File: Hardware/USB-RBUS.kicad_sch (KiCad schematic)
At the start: 8 parts, among them J4 USB_C_Receptacle_USB2.0

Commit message: PCB mid design
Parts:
- removed D6: SP0503BAHT, Package_TO_SOT_SMD:SOT-143, symbol Power_Protection:SP0503BAHT
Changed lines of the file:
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@@
-	(wire
-		(pts
-			(xy 124.46 91.44) (xy 124.46 97.79)
-		)
-		(stroke
-			(width 0)
-			(type default)
-		)
-	)
 	(wire
 		(pts
@@
 			)
 			(justify left bottom)
-		)
-	)
-	(label "CAN+"
-		(at 129.54 97.79 90)
-		(fields_autoplaced yes)
-		(effects
-			(font
-				(size 1.27 1.27)
-			)
-			(justify left bottom)
-		)
-	)
-	(label "CAN-"
-		(at 127 97.79 90)
-		(fields_autoplaced yes)
-		(effects
-			(font
-				(size 1.27 1.27)
-			)
-			(justify left bottom)
-		)
-	)
-	(global_label "RBUS_uC_V"
-		(shape input)
-		(at 124.46 91.44 90)
-		(fields_autoplaced yes)
-		(effects
-			(font
-				(size 1.27 1.27)
-			)
-			(justify left)
-		)
-		(property "Intersheetrefs" "${INTERSHEET_REFS}"
-			(at 124.46 78.5862 90)
-			(effects
-				(font
-					(size 1.27 1.27)
-				)
-				(justify left)
-				(hide yes)
-			)
 		)
 	)
@@
 					(unit 1)
 				)
-			)
-		)
-	)
-	(symbol
-		(lib_id "power:GND")
-		(at 127 107.95 0)
-		(unit 1)
-		(exclude_from_sim no)
-		(in_bom yes)
-		(on_board yes)
-		(dnp no)
-		(property "Reference" "#PWR062"
-			(at 127 114.3 0)
-			(effects
-				(font
-					(size 1.27 1.27)
-				)
-				(hide yes)
-			)
-		)
-		(property "Value" "GND"
-			(at 127.127 112.3442 0)
-			(effects
-				(font
-					(size 1.27 1.27)
-				)
-			)
-		)
-		(property "Footprint" ""
-			(at 127 107.95 0)
-			(effects
-				(font
-					(size 1.27 1.27)
-				)
-				(hide yes)
-			)
-		)
-		(property "Datasheet" ""
-			(at 127 107.95 0)
-			(effects
-				(font
-					(size 1.27 1.27)
-				)
-				(hide yes)
-			)
-		)
-		(property "Description" ""
-			(at 127 107.95 0)
-			(effects
-				(font
-					(size 1.27 1.27)
-				)
-				(hide yes)
-			)
-		)
-		(pin "1"
-		)
-		(instances
-			(project "Main board"
-				(path "/7db990e4-92e1-4f99-b4d2-435bbec1ba83/3151accb-1938-449b-8397-baa4e59e1635"
-					(reference "#PWR062")
-					(unit 1)
-				)
-			)
-		)
-	)
-	(symbol
-		(lib_id "Power_Protection:SP0503BAHT")
-		(at 127 102.87 0)
-		(unit 1)
-		(exclude_from_sim no)
-		(in_bom yes)
-		(on_board yes)
-		(dnp no)
-		(property "Reference" "D6"
-			(at 132.207 101.7016 0)
-			(effects
-				(font
-					(size 1.27 1.27)
-				)
-				(justify left)
-			)
-		)
-		(property "Value" "SP0503BAHT"
-			(at 132.207 104.013 0)
-			(effects
-				(font
-					(size 1.27 1.27)
-				)
-				(justify left)
-			)
-		)
-		(property "Footprint" "Package_TO_SOT_SMD:SOT-143"
-			(at 132.715 104.14 0)
-			(effects
-				(font
-					(size 1.27 1.27)
-				)
-				(justify left)
-				(hide yes)
-			)
-		)
-		(property "Datasheet" "http://www.littelfuse.com/~/media/files/littelfuse/technical%20resources/documents/data%20sheets/sp05xxba.pdf"
-			(at 130.175 99.695 0)
-			(effects
-				(font
-					(size 1.27 1.27)
-				)
-				(hide yes)
-			)
-		)
-		(property "Description" ""
-			(at 127 102.87 0)
-			(effects
-				(font
-					(size 1.27 1.27)
-				)
-				(hide yes)
-			)
-		)
-		(pin "1"
-		)
-		(pin "2"
-		)
-		(pin "3"
-		)
-		(pin "4"
-		)
-		(instances
-			(project "Main board"
-				(path "/7db990e4-92e1-4f99-b4d2-435bbec1ba83/3151accb-1938-449b-8397-baa4e59e1635"
-					(reference "D6")
-					(unit 1)
-				)

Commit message: Crosshair V1.0
New pyro connectors, silkscreen sorted, mostly connected properly + cool new name and image
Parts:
- J4: footprint Connector_USB:USB_C_Receptacle_Palconn_UTC16-G -> iclr:USB_C_Receptacle_Palconn_UTC16-G
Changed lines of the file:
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@@
 (kicad_sch
-	(version 20231120)
+	(version 20250114)
 	(generator "eeschema")
-	(generator_version "8.0")
+	(generator_version "9.0")
 	(paper "A4")
 	(junction
@@
 	(label "CAN+"
 		(at 39.37 67.31 0)
-		(fields_autoplaced yes)
 		(effects
 			(font
@@
 	(label "CAN-"
 		(at 111.76 66.04 0)
-		(fields_autoplaced yes)
 		(effects
 			(font
@@
 	(label "CAN-"
 		(at 39.37 62.23 0)
-		(fields_autoplaced yes)
 		(effects
 			(font
@@
 	(label "CAN+"
 		(at 111.76 71.12 0)
-		(fields_autoplaced yes)
 		(effects
 			(font
@@
 		(shape bidirectional)
 		(at 39.37 67.31 180)
-		(fields_autoplaced yes)
 		(effects
 			(font
@@
 		(shape bidirectional)
 		(at 39.37 62.23 180)
-		(fields_autoplaced yes)
 		(effects
 			(font
@@
 			)
 		)
-		(property "Footprint" "Connector_USB:USB_C_Receptacle_Palconn_UTC16-G"
+		(property "Footprint" "iclr:USB_C_Receptacle_Palconn_UTC16-G"
 			(at 99.06 67.31 0)
 			(effects

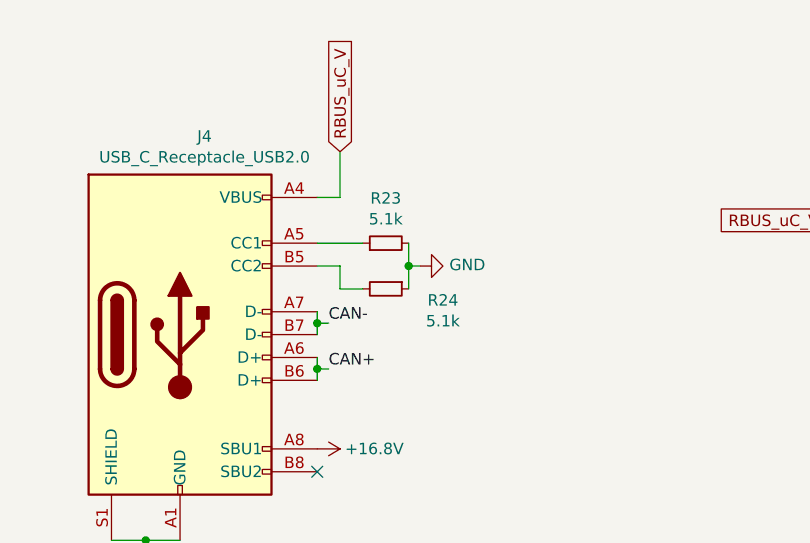
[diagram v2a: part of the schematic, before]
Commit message: Crosshair post review 2
Layout redesign + changes implemented. Traces not yet complete
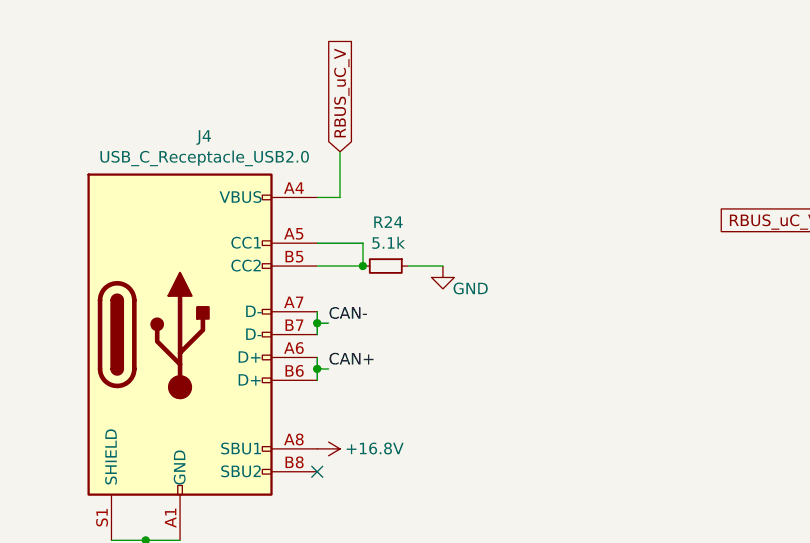
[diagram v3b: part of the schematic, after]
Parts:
- removed R23: 5.1k, Resistor_SMD:R_0402_1005Metric, symbol Device:R_Small
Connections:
- net at J4.A5 (CC1): now also J4.B5 (CC2), R24.2
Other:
- moved on the sheet: R24
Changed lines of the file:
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@@
 	)
 	(junction
-		(at 120.65 59.69)
+		(at 115.57 59.69)
 		(diameter 0)
 		(color 0 0 0 0)
@@
 	(wire
 		(pts
-			(xy 110.49 59.69) (xy 113.03 59.69)
+			(xy 110.49 59.69) (xy 115.57 59.69)
 		)
 		(stroke
@@
 	(wire
 		(pts
-			(xy 120.65 59.69) (xy 121.92 59.69)
+			(xy 120.65 59.69) (xy 124.46 59.69)
+		)
+		(stroke
+			(width 0)
+			(type default)
+		)
+	)
+	(wire
+		(pts
+			(xy 115.57 57.15) (xy 115.57 59.69)
 		)
 		(stroke
@@
 	(wire
 		(pts
-			(xy 113.03 62.23) (xy 115.57 62.23)
-		)
-		(stroke
-			(width 0)
-			(type default)
-		)
-	)
-	(wire
-		(pts
-			(xy 120.65 57.15) (xy 120.65 59.69)
-		)
-		(stroke
-			(width 0)
-			(type default)
-		)
-	)
-	(wire
-		(pts
 			(xy 110.49 71.12) (xy 110.49 72.39)
 		)
@@
 	(wire
 		(pts
-			(xy 113.03 59.69) (xy 113.03 62.23)
-		)
-		(stroke
-			(width 0)
-			(type default)
-		)
-	)
-	(wire
-		(pts
 			(xy 87.63 90.17) (xy 91.44 90.17)
 		)
@@
 		(pts
 			(xy 110.49 69.85) (xy 110.49 71.12)
-		)
-		(stroke
-			(width 0)
-			(type default)
-		)
-	)
-	(wire
-		(pts
-			(xy 120.65 62.23) (xy 120.65 59.69)
 		)
 		(stroke
@@
 			)
 			(justify right)
-		)
-	)
-	(symbol
-		(lib_id "Device:R_Small")
-		(at 118.11 57.15 90)
-		(unit 1)
-		(exclude_from_sim no)
-		(in_bom yes)
-		(on_board yes)
-		(dnp no)
-		(property "Reference" "R23"
-			(at 118.11 52.1716 90)
-			(effects
-				(font
-					(size 1.27 1.27)
-				)
-			)
-		)
-		(property "Value" "5.1k"
-			(at 118.11 54.483 90)
-			(effects
-				(font
-					(size 1.27 1.27)
-				)
-			)
-		)
-		(property "Footprint" "Resistor_SMD:R_0402_1005Metric"
-			(at 118.11 57.15 0)
-			(effects
-				(font
-					(size 1.27 1.27)
-				)
-				(hide yes)
-			)
-		)
-		(property "Datasheet" "~"
-			(at 118.11 57.15 0)
-			(effects
-				(font
-					(size 1.27 1.27)
-				)
-				(hide yes)
-			)
-		)
-		(property "Description" ""
-			(at 118.11 57.15 0)
-			(effects
-				(font
-					(size 1.27 1.27)
-				)
-				(hide yes)
-			)
-		)
-		(pin "1"
-		)
-		(pin "2"
-		)
-		(instances
-			(project "Main board"
-				(path "/7db990e4-92e1-4f99-b4d2-435bbec1ba83/3151accb-1938-449b-8397-baa4e59e1635"
-					(reference "R23")
-					(unit 1)
-				)
-			)
 		)
 	)
@@
 	(symbol
 		(lib_id "power:GND")
-		(at 121.92 59.69 90)
+		(at 124.46 59.69 0)
 		(unit 1)
 		(exclude_from_sim no)
@@
 		(dnp no)
 		(property "Reference" "#PWR060"
-			(at 128.27 59.69 0)
+			(at 124.46 66.04 0)
 			(effects
 				(font
@@
 		)
 		(property "Value" "GND"
-			(at 125.1712 59.563 90)
+			(at 129.54 62.23 0)
 			(effects
 				(font
@@
 		)
 		(property "Footprint" ""
-			(at 121.92 59.69 0)
+			(at 124.46 59.69 0)
 			(effects
 				(font
@@
 		)
 		(property "Datasheet" ""
-			(at 121.92 59.69 0)
+			(at 124.46 59.69 0)
 			(effects
 				(font
@@
 		)
 		(property "Description" ""
-			(at 121.92 59.69 0)
+			(at 124.46 59.69 0)
 			(effects
 				(font
@@
 	(symbol
 		(lib_id "Device:R_Small")
-		(at 118.11 62.23 270)
+		(at 118.11 59.69 270)
 		(unit 1)
 		(exclude_from_sim no)
@@
 		(dnp no)
 		(property "Reference" "R24"
-			(at 124.46 63.5 90)
+			(at 118.364 54.864 90)
 			(effects
 				(font
@@
 		)
 		(property "Value" "5.1k"
-			(at 124.46 65.8114 90)
+			(at 118.364 57.1754 90)
 			(effects
 				(font
@@
 		)
 		(property "Footprint" "Resistor_SMD:R_0402_1005Metric"
-			(at 118.11 62.23 0)
+			(at 118.11 59.69 0)
 			(effects
 				(font
@@
 		)
 		(property "Datasheet" "~"
-			(at 118.11 62.23 0)
+			(at 118.11 59.69 0)
 			(effects
 				(font
@@
 		)
 		(property "Description" ""
-			(at 118.11 62.23 0)
-			(effects
-				(font
+			(at 118.11 59.69 0)
+			(effects
+				(font

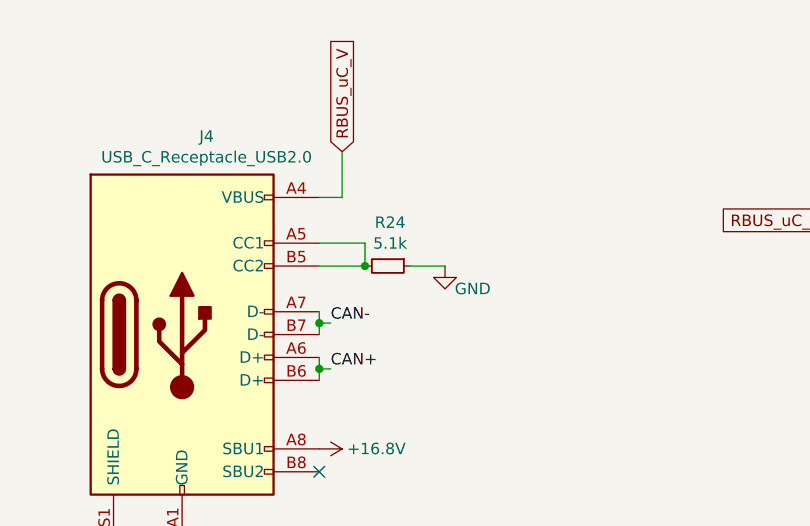
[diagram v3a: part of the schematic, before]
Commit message: I2C 'bus' sorted
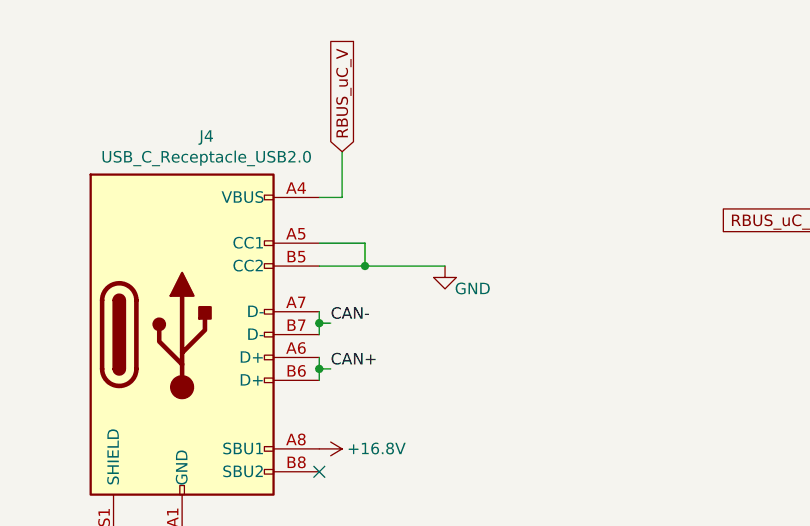
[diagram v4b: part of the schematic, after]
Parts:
- removed R24: 5.1k, Resistor_SMD:R_0402_1005Metric, symbol Device:R_Small
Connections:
- net GND: now also J4.A5 (CC1), J4.B5 (CC2)
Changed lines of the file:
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@@
+	)
+	(junction
+		(at 110.49 71.12)
+		(diameter 0)
+		(color 0 0 0 0)
 	)
 	(junction
@@
 	)
 	(junction
-		(at 110.49 71.12)
-		(diameter 0)
-		(color 0 0 0 0)
-	)
-	(junction
 		(at 91.44 90.17)
 		(diameter 0)
@@
 	(wire
 		(pts
-			(xy 120.65 59.69) (xy 124.46 59.69)
-		)
-		(stroke
-			(width 0)
-			(type default)
-		)
-	)
-	(wire
-		(pts
 			(xy 115.57 57.15) (xy 115.57 59.69)
 		)
@@
 		(pts
 			(xy 110.49 67.31) (xy 110.49 66.04)
+		)
+		(stroke
+			(width 0)
+			(type default)
+		)
+	)
+	(wire
+		(pts
+			(xy 115.57 59.69) (xy 124.46 59.69)
 		)
 		(stroke
@@
 					(unit 1)
 				)
-			)
-		)
-	)
-	(symbol
-		(lib_id "Device:R_Small")
-		(at 118.11 59.69 270)
-		(unit 1)
-		(exclude_from_sim no)
-		(in_bom yes)
-		(on_board yes)
-		(dnp no)
-		(property "Reference" "R24"
-			(at 118.364 54.864 90)
-			(effects
-				(font
-					(size 1.27 1.27)
-				)
-			)
-		)
-		(property "Value" "5.1k"
-			(at 118.364 57.1754 90)
-			(effects
-				(font
-					(size 1.27 1.27)
-				)
-			)
-		)
-		(property "Footprint" "Resistor_SMD:R_0402_1005Metric"
-			(at 118.11 59.69 0)
-			(effects
-				(font
-					(size 1.27 1.27)
-				)
-				(hide yes)
-			)
-		)
-		(property "Datasheet" "~"
-			(at 118.11 59.69 0)
-			(effects
-				(font
-					(size 1.27 1.27)
-				)
-				(hide yes)
-			)
-		)
-		(property "Description" ""
-			(at 118.11 59.69 0)
-			(effects
-				(font
-					(size 1.27 1.27)
-				)
-				(hide yes)
-			)
-		)
-		(pin "1"
-		)
-		(pin "2"
-		)
-		(instances
-			(project "Main board"
-				(path "/7db990e4-92e1-4f99-b4d2-435bbec1ba83/3151accb-1938-449b-8397-baa4e59e1635"
-					(reference "R24")
-					(unit 1)
-				)

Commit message: Mega commit
Post review changes
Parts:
- RBUSLED: renamed from USBLED2; footprint Resistor_SMD:R_0402_1005Metric -> LED_SMD:LED_0402_1005Metric
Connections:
- net +16.8V: now also J4.A4 (VBUS), J4.A9 (VBUS), J4.B4 (VBUS), J4.B9 (VBUS); no longer J4.A8 (SBU1)
- net GND: no longer J4.A5 (CC1), J4.B5 (CC2)
- net RBUS_uC_V: now also J4.A5 (CC1), J4.B5 (CC2); no longer J4.A4 (VBUS), J4.A9 (VBUS), J4.B4 (VBUS), J4.B9 (VBUS)
- no-connect marks 1 -> 2
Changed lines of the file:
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@@
 	)
 	(junction
-		(at 115.57 59.69)
+		(at 110.49 58.42)
 		(diameter 0)
 		(color 0 0 0 0)
@@
 		(at 110.49 82.55)
 	)
+	(no_connect
+		(at 110.49 80.01)
+	)
 	(wire
 		(pts
@@
 	(wire
 		(pts
-			(xy 110.49 59.69) (xy 115.57 59.69)
-		)
-		(stroke
-			(width 0)
-			(type default)
-		)
-	)
-	(wire
-		(pts
 			(xy 110.49 66.04) (xy 110.49 64.77)
 		)
@@
 	(wire
 		(pts
-			(xy 110.49 57.15) (xy 115.57 57.15)
-		)
-		(stroke
-			(width 0)
-			(type default)
-		)
-	)
-	(wire
-		(pts
-			(xy 115.57 57.15) (xy 115.57 59.69)
+			(xy 110.49 57.15) (xy 110.49 58.42)
+		)
+		(stroke
+			(width 0)
+			(type default)
+		)
+	)
+	(wire
+		(pts
+			(xy 110.49 58.42) (xy 111.76 58.42)
 		)
 		(stroke
@@
 	(wire
 		(pts
-			(xy 115.57 59.69) (xy 124.46 59.69)
+			(xy 110.49 58.42) (xy 110.49 59.69)
 		)
 		(stroke
@@
 	(global_label "RBUS_uC_V"
 		(shape input)
-		(at 113.03 46.99 90)
+		(at 111.76 58.42 0)
 		(fields_autoplaced yes)
 		(effects
@@
 		)
 		(property "Intersheetrefs" "${INTERSHEET_REFS}"
-			(at 113.03 34.1362 90)
+			(at 124.6138 58.42 0)
 			(effects
 				(font
@@
 			)
 			(justify right)
-		)
-	)
-	(symbol
-		(lib_id "power:+12V")
-		(at 110.49 80.01 270)
-		(mirror x)
-		(unit 1)
-		(exclude_from_sim no)
-		(in_bom yes)
-		(on_board yes)
-		(dnp no)
-		(property "Reference" "#PWR059"
-			(at 106.68 80.01 0)
-			(effects
-				(font
-					(size 1.27 1.27)
-				)
-				(hide yes)
-			)
-		)
-		(property "Value" "+16.8V"
-			(at 116.84 80.01 90)
-			(effects
-				(font
-					(size 1.27 1.27)
-				)
-			)
-		)
-		(property "Footprint" ""
-			(at 110.49 80.01 0)
-			(effects
-				(font
-					(size 1.27 1.27)
-				)
-				(hide yes)
-			)
-		)
-		(property "Datasheet" ""
-			(at 110.49 80.01 0)
-			(effects
-				(font
-					(size 1.27 1.27)
-				)
-				(hide yes)
-			)
-		)
-		(property "Description" ""
-			(at 110.49 80.01 0)
-			(effects
-				(font
-					(size 1.27 1.27)
-				)
-				(hide yes)
-			)
-		)
-		(pin "1"
-		)
-		(instances
-			(project "Main board"
-				(path "/7db990e4-92e1-4f99-b4d2-435bbec1ba83/3151accb-1938-449b-8397-baa4e59e1635"
-					(reference "#PWR059")
-					(unit 1)
-				)
-			)
 		)
 	)
@@
 		(on_board yes)
 		(dnp no)
-		(property "Reference" "USBLED2"
+		(property "Reference" "RBUSLED"
 			(at 179.07 49.403 0)
 			(effects
@@
 			)
 		)
-		(property "Footprint" "Resistor_SMD:R_0402_1005Metric"
+		(property "Footprint" "LED_SMD:LED_0402_1005Metric"
 			(at 179.07 54.61 90)
 			(effects
@@
 			(project "Main board"
 				(path "/7db990e4-92e1-4f99-b4d2-435bbec1ba83/3151accb-1938-449b-8397-baa4e59e1635"
-					(reference "USBLED2")
+					(reference "RBUSLED")
 					(unit 1)
 				)
@@
 	)
 	(symbol
-		(lib_id "power:GND")
-		(at 124.46 59.69 0)
+		(lib_id "power:+12V")
+		(at 113.03 46.99 0)
+		(mirror y)
 		(unit 1)
 		(exclude_from_sim no)
@@
 		(on_board yes)
 		(dnp no)
-		(property "Reference" "#PWR060"
-			(at 124.46 66.04 0)
-			(effects
-				(font
-					(size 1.27 1.27)
-				)
-				(hide yes)
-			)
-		)
-		(property "Value" "GND"
-			(at 129.54 62.23 0)
-			(effects
-				(font
-					(size 1.27 1.27)
-				)
-				(justify right)
+		(property "Reference" "#PWR067"
+			(at 113.03 50.8 0)
+			(effects
+				(font
+					(size 1.27 1.27)
+				)
+				(hide yes)
+			)
+		)
+		(property "Value" "+16.8V"
+			(at 117.602 45.466 0)
+			(effects
+				(font
+					(size 1.27 1.27)
+				)
 			)
 		)
 		(property "Footprint" ""
-			(at 124.46 59.69 0)
+			(at 113.03 46.99 0)
 			(effects
 				(font
@@
 		)
 		(property "Datasheet" ""
-			(at 124.46 59.69 0)
+			(at 113.03 46.99 0)
 			(effects
 				(font
@@
 		)
 		(property "Description" ""
-			(at 124.46 59.69 0)
+			(at 113.03 46.99 0)
 			(effects
 				(font
@@
 			(project "Main board"
 				(path "/7db990e4-92e1-4f99-b4d2-435bbec1ba83/3151accb-1938-449b-8397-baa4e59e1635"
-					(reference "#PWR060")
+					(reference "#PWR067")
 					(unit 1)
 				)

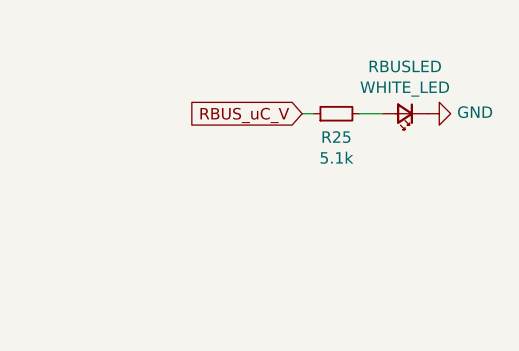
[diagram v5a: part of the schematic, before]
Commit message: Silkscreen label
Made sure PCB file was saved before push...
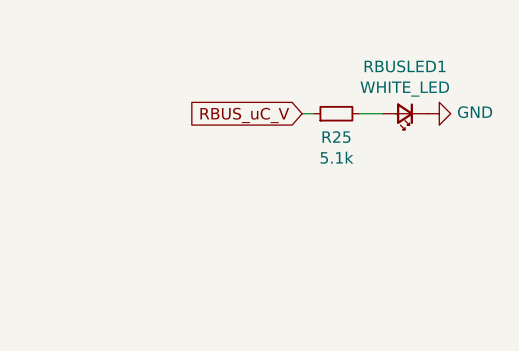
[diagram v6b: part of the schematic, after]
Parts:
- renumbered RBUSLED to RBUSLED1
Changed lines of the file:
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@@
 		(on_board yes)
 		(dnp no)
-		(property "Reference" "RBUSLED"
+		(property "Reference" "RBUSLED1"
 			(at 179.07 49.403 0)
 			(effects
@@
 			(project "Main board"
 				(path "/7db990e4-92e1-4f99-b4d2-435bbec1ba83/3151accb-1938-449b-8397-baa4e59e1635"
-					(reference "RBUSLED")
+					(reference "RBUSLED1")
 					(unit 1)
 				)

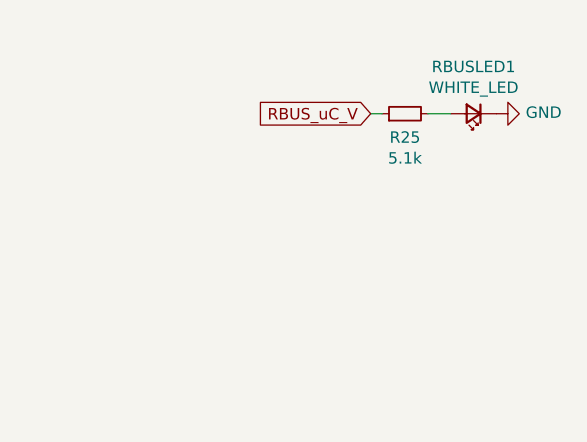
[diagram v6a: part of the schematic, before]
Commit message: More V2 changes
Mainly changed to use Ω symbol for resistors. Fixed the CDC pin for the buck boost
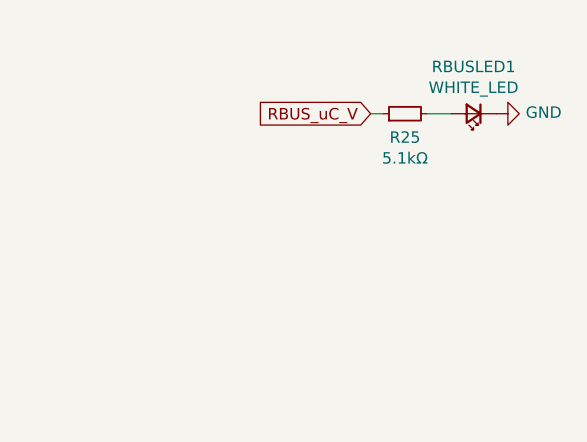
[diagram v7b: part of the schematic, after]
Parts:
- R25: value 5.1k -> 5.1kΩ
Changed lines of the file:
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@@
 			)
 		)
-		(property "Value" "5.1k"
+		(property "Value" "5.1kΩ"
 			(at 171.45 59.563 90)
 			(effects

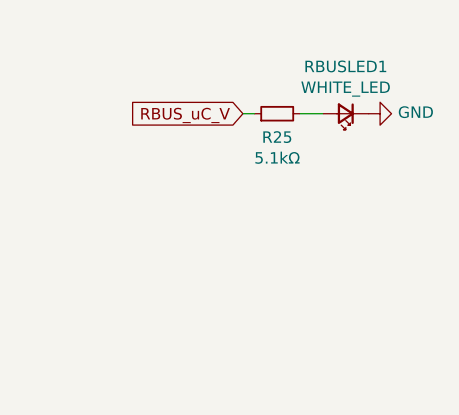
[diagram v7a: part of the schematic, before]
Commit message: Post second Jack review
Adopted most changes
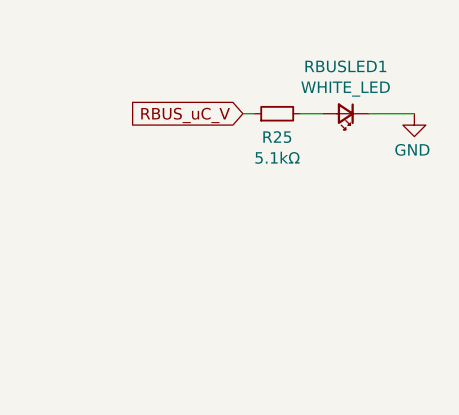
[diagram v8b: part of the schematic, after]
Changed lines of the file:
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@@
+	(wire
+		(pts
+			(xy 186.69 54.61) (xy 181.61 54.61)
+		)
+		(stroke
+			(width 0)
+			(type default)
+		)
+	)
 	(wire
 		(pts
@@
 	(symbol
 		(lib_id "power:GND")
-		(at 181.61 54.61 90)
+		(at 186.69 54.61 0)
 		(unit 1)
 		(exclude_from_sim no)
@@
 		(dnp no)
 		(property "Reference" "#PWR064"
-			(at 187.96 54.61 0)
+			(at 186.69 60.96 0)
 			(effects
 				(font
@@
 		)
 		(property "Value" "GND"
-			(at 184.8612 54.483 90)
+			(at 188.468 58.674 0)
 			(effects
 				(font
@@
 		)
 		(property "Footprint" ""
-			(at 181.61 54.61 0)
+			(at 186.69 54.61 0)
 			(effects
 				(font
@@
 		)
 		(property "Datasheet" ""
-			(at 181.61 54.61 0)
+			(at 186.69 54.61 0)
 			(effects
 				(font
@@
 		)
 		(property "Description" ""
-			(at 181.61 54.61 0)
-			(effects
-				(font
+			(at 186.69 54.61 0)
+			(effects
+				(font
